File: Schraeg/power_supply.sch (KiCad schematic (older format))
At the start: 30 parts, among them U1 TL074, U2 TL074, U3 V2164, U4 TL074, U5 TL074

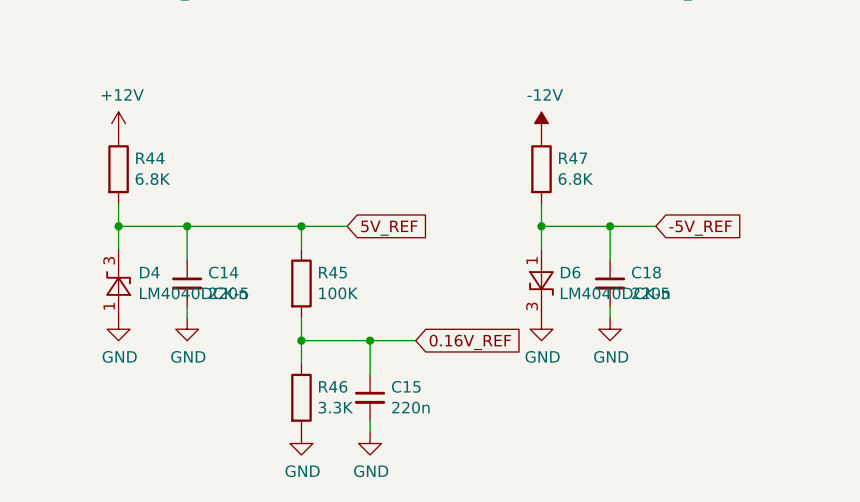
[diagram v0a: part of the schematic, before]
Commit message: Fixed LM4040 symbols and PCB layout. Fixes #2
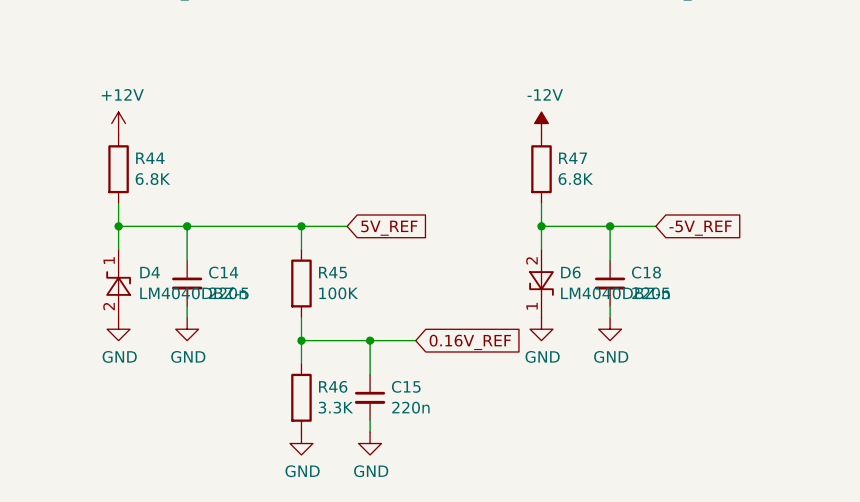
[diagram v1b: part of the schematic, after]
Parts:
- removed D4, D6: LM4040DCK-5, Package_TO_SOT_SMD:SOT-23_Handsoldering, symbol Reference_Voltage:LM4040DCK-5
- added D4, D6: LM4040DBZ-5, Package_TO_SOT_SMD:SOT-23, symbol Reference_Voltage:LM4040DBZ-5
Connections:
- net -5V_REF: now also D6.2 (A)
- net 5V_REF: now also D4.1 (K)
- net GND: now also D4.2 (A), D6.1 (K)
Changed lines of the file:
@@
 	2150 3200 2150 3100
-$Comp
-L Reference_Voltage:LM4040DCK-5 D?
-U 1 1 5DA7E231
-P 3200 3350
-AR Path="/5DA7E231" Ref="D?"  Part="1"
-AR Path="/5DA7C710/5DA7E231" Ref="D6"  Part="1"
-F 0 "D6" V 3154 3428 50  0000 L CNN
-F 1 "LM4040DCK-5" V 3245 3428 50  0000 L CNN
-F 2 "Package_TO_SOT_SMD:SOT-23_Handsoldering" H 3200 3150 50  0001 C CIN
-F 3 "http://www.ti.com/lit/ds/symlink/lm4040-n.pdf" H 3200 3350 50  0001 C CIN
-	1    3200 3350
-	0    1    1    0
-$EndComp
 $Comp
 L Device:R R?
@@
 Wire Wire Line
 	3500 3100 3700 3100
-$Comp
-L Reference_Voltage:LM4040DCK-5 D?
-U 1 1 5DA7E272
-P 1350 3350
-AR Path="/5DA7E272" Ref="D?"  Part="1"
-AR Path="/5DA7C710/5DA7E272" Ref="D4"  Part="1"
-F 0 "D4" V 1396 3263 50  0000 R CNN
-F 1 "LM4040DCK-5" V 1305 3263 50  0000 R CNN
-F 2 "Package_TO_SOT_SMD:SOT-23_Handsoldering" H 1350 3150 50  0001 C CIN
-F 3 "http://www.ti.com/lit/ds/symlink/lm4040-n.pdf" H 1350 3350 50  0001 C CIN
-	1    1350 3350
-	0    -1   -1   0
-$EndComp
 $Comp
 L Device:R R?
@@
 Wire Wire Line
 	3850 1900 4550 1900
+$Comp
+L Reference_Voltage:LM4040DBZ-5 D6
+U 1 1 60B20A30
+P 3200 3350
+F 0 "D6" V 3154 3429 50  0000 L CNN
+F 1 "LM4040DBZ-5" V 3245 3429 50  0000 L CNN
+F 2 "Package_TO_SOT_SMD:SOT-23" H 3200 3150 50  0001 C CIN
+F 3 "http://www.ti.com/lit/ds/symlink/lm4040-n.pdf" H 3200 3350 50  0001 C CIN
+	1    3200 3350
+	0    1    1    0
+$EndComp
+$Comp
+L Reference_Voltage:LM4040DBZ-5 D4
+U 1 1 60B343BC
+P 1350 3350
+F 0 "D4" V 1396 3262 50  0000 R CNN
+F 1 "LM4040DBZ-5" V 1305 3262 50  0000 R CNN
+F 2 "Package_TO_SOT_SMD:SOT-23" H 1350 3150 50  0001 C CIN
+F 3 "http://www.ti.com/lit/ds/symlink/lm4040-n.pdf" H 1350 3350 50  0001 C CIN
+	1    1350 3350
+	0    -1   -1   0
+$EndComp
 $EndSCHEMATC
